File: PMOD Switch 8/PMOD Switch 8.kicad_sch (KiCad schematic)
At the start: 9 parts, among them SW1 SW_DIP_x08

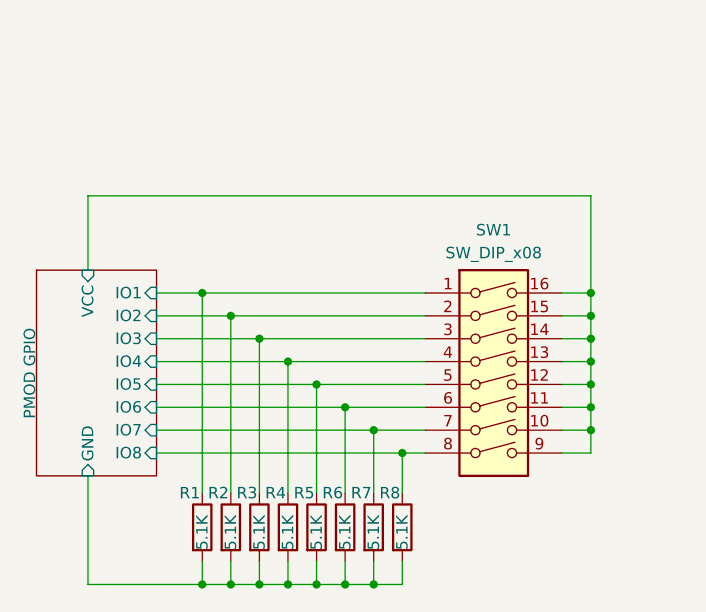
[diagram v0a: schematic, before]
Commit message: 添加了新的PMOD 模块
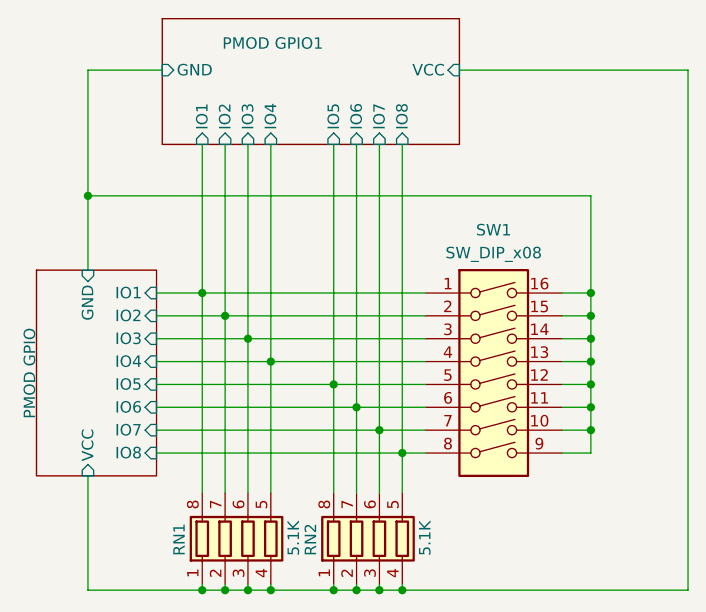
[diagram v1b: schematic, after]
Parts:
- removed R1, R2, R3, R4, R5, R6, R7, R8: 5.1K, symbol Device:R
- added RN1, RN2: 5.1K, Resistor_SMD:R_Array_Convex_4x0603, symbol Device:R_Pack04
- SW1: footprint (none) -> Button_Switch_SMD:SW_DIP_SPSTx08_Slide_6.7x21.88mm_W8.61mm_P2.54mm_LowProfile
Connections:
- net PMOD GPIO/GND: now also SW1.10, SW1.11, SW1.12, SW1.13, SW1.14, SW1.15, SW1.16, SW1.9
- net PMOD GPIO/IO1: now also RN1.8 (R1.2)
- net PMOD GPIO/IO2: now also RN1.7 (R2.2)
- net PMOD GPIO/IO3: now also RN1.6 (R3.2)
- net PMOD GPIO/IO4: now also RN1.5 (R4.2)
- net PMOD GPIO/IO5: now also RN2.8 (R1.2)
- net PMOD GPIO/IO6: now also RN2.7 (R2.2)
- net PMOD GPIO/IO7: now also RN2.6 (R3.2)
- net PMOD GPIO/IO8: now also RN2.5 (R4.2)
- net PMOD GPIO/VCC: now also RN1.1 (R1.1), RN1.2 (R2.1), RN1.3 (R3.1), RN1.4 (R4.1), RN2.1 (R1.1), RN2.2 (R2.1), RN2.3 (R3.1), RN2.4 (R4.1); no longer SW1.10, SW1.11, SW1.12, SW1.13, SW1.14, SW1.15, SW1.16, SW1.9
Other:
- added sheet PMOD GPIO1 (C:/Users/tbz/OneDrive/doc/kicad_schematic/pmod_gpio.kicad_sch)
